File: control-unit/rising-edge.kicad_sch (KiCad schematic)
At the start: 0 parts

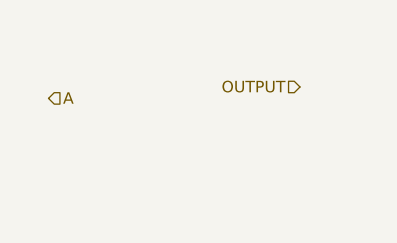
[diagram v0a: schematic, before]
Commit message: Rising edge diagram
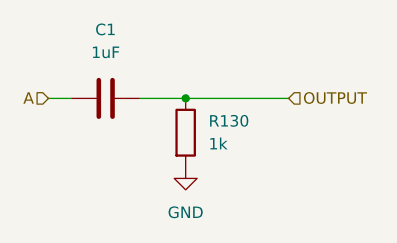
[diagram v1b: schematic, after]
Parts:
- added C1: 1uF, symbol Device:C
- added R130: 1k, symbol Device:R
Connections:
- net A: now also C1.1
- net OUTPUT: now also C1.2, R130.1
- new net GND: R130.2
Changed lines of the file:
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@@
 	(generator_version "8.0")
 	(paper "A4")
+	(junction
+		(at 110.49 80.01)
+		(diameter 0)
+		(color 0 0 0 0)
+	)
+	(wire
+		(pts
+			(xy 105.41 80.01) (xy 110.49 80.01)
+		)
+		(stroke
+			(width 0)
+			(type default)
+		)
+	)
+	(wire
+		(pts
+			(xy 95.25 80.01) (xy 97.79 80.01)
+		)
+		(stroke
+			(width 0)
+			(type default)
+		)
+	)
+	(wire
+		(pts
+			(xy 110.49 80.01) (xy 121.92 80.01)
+		)
+		(stroke
+			(width 0)
+			(type default)
+		)
+	)
 	(hierarchical_label "A"
 		(shape input)
-		(at 95.25 80.01 0)
+		(at 95.25 80.01 180)
 		(fields_autoplaced yes)
 		(effects
@@
 				(size 1.27 1.27)
 			)
-			(justify left)
+			(justify right)
 		)
 	)
 	(hierarchical_label "OUTPUT"
 		(shape input)
-		(at 123.19 78.74 180)
+		(at 121.92 80.01 0)
 		(fields_autoplaced yes)
 		(effects
@@
 				(size 1.27 1.27)
 			)
-			(justify right)
-		)
-	)
+			(justify left)
+		)
+	)
+	(symbol
+		(lib_id "Device:R")
+		(at 110.49 83.82 0)
+		(unit 1)
+		(exclude_from_sim no)
+		(in_bom yes)
+		(on_board yes)
+		(dnp no)
+		(fields_autoplaced yes)
+		(property "Reference" "R130"
+			(at 113.03 82.5499 0)
+			(effects
+				(font
+					(size 1.27 1.27)
+				)
+				(justify left)
+			)
+		)
+		(property "Value" "1k"
+			(at 113.03 85.0899 0)
+			(effects
+				(font
+					(size 1.27 1.27)
+				)
+				(justify left)
+			)
+		)
+		(property "Footprint" ""
+			(at 108.712 83.82 90)
+			(effects
+				(font
+					(size 1.27 1.27)
+				)
+				(hide yes)
+			)
+		)
+		(property "Datasheet" "~"
+			(at 110.49 83.82 0)
+			(effects
+				(font
+					(size 1.27 1.27)
+				)
+				(hide yes)
+			)
+		)
+		(property "Description" "Resistor"
+			(at 110.49 83.82 0)
+			(effects
+				(font
+					(size 1.27 1.27)
+				)
+				(hide yes)
+			)
+		)
+		(pin "2"
+		)
+		(pin "1"
+		)
+		(instances
+			(project ""
+				(path "/1cf3a7ee-ec47-45b6-b515-1840d726ab8f/de2e1405-3239-4ce6-b747-5c12d2d075a5"
+					(reference "R130")
+					(unit 1)
+				)
+			)
+		)
+	)
+	(symbol
+		(lib_id "Device:C")
+		(at 101.6 80.01 90)
+		(unit 1)
+		(exclude_from_sim no)
+		(in_bom yes)
+		(on_board yes)
+		(dnp no)
+		(fields_autoplaced yes)
+		(property "Reference" "C1"
+			(at 101.6 72.39 90)
+			(effects
+				(font
+					(size 1.27 1.27)
+				)
+			)
+		)
+		(property "Value" "1uF"
+			(at 101.6 74.93 90)
+			(effects
+				(font
+					(size 1.27 1.27)
+				)
+			)
+		)
+		(property "Footprint" ""
+			(at 105.41 79.0448 0)
+			(effects
+				(font
+					(size 1.27 1.27)
+				)
+				(hide yes)
+			)
+		)
+		(property "Datasheet" "~"
+			(at 101.6 80.01 0)
+			(effects
+				(font
+					(size 1.27 1.27)
+				)
+				(hide yes)
+			)
+		)
+		(property "Description" "Unpolarized capacitor"
+			(at 101.6 80.01 0)
+			(effects
+				(font
+					(size 1.27 1.27)
+				)
+				(hide yes)
+			)
+		)
+		(pin "2"
+		)
+		(pin "1"
+		)
+		(instances
+			(project ""
+				(path "/1cf3a7ee-ec47-45b6-b515-1840d726ab8f/de2e1405-3239-4ce6-b747-5c12d2d075a5"
+					(reference "C1")
+					(unit 1)
+				)
+			)
+		)
+	)
+	(symbol
+		(lib_id "power:GND")
+		(at 110.49 87.63 0)
+		(unit 1)
+		(exclude_from_sim no)
+		(in_bom yes)
+		(on_board yes)
+		(dnp no)
+		(fields_autoplaced yes)
+		(property "Reference" "#PWR047"
+			(at 110.49 93.98 0)
+			(effects
+				(font
+					(size 1.27 1.27)
+				)
+				(hide yes)
+			)
+		)
+		(property "Value" "GND"
+			(at 110.49 92.71 0)
+			(effects
+				(font
+					(size 1.27 1.27)
+				)
+			)
+		)
+		(property "Footprint" ""
+			(at 110.49 87.63 0)
+			(effects
+				(font
+					(size 1.27 1.27)
+				)
+				(hide yes)
+			)
+		)
+		(property "Datasheet" ""
+			(at 110.49 87.63 0)
+			(effects
+				(font
+					(size 1.27 1.27)
+				)
+				(hide yes)
+			)
+		)
+		(property "Description" "Power symbol creates a global label with name \"GND\" , ground"
+			(at 110.49 87.63 0)
+			(effects
+				(font
+					(size 1.27 1.27)
+				)
+				(hide yes)
+			)
+		)
+		(pin "1"
+		)
+		(instances
+			(project ""
+				(path "/1cf3a7ee-ec47-45b6-b515-1840d726ab8f/de2e1405-3239-4ce6-b747-5c12d2d075a5"
+					(reference "#PWR047")
+					(unit 1)
+				)
+			)
+		)
+	)
